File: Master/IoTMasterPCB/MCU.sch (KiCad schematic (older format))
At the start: 1 part

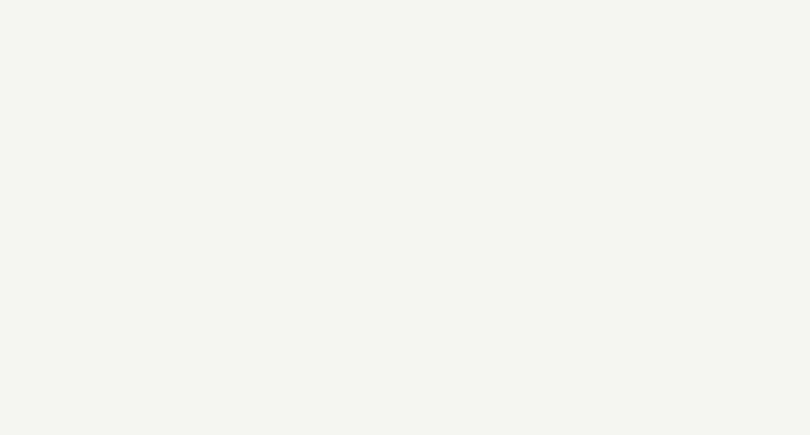
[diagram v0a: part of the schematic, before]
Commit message: Updated Master Board schematics. Added JTAG connector.
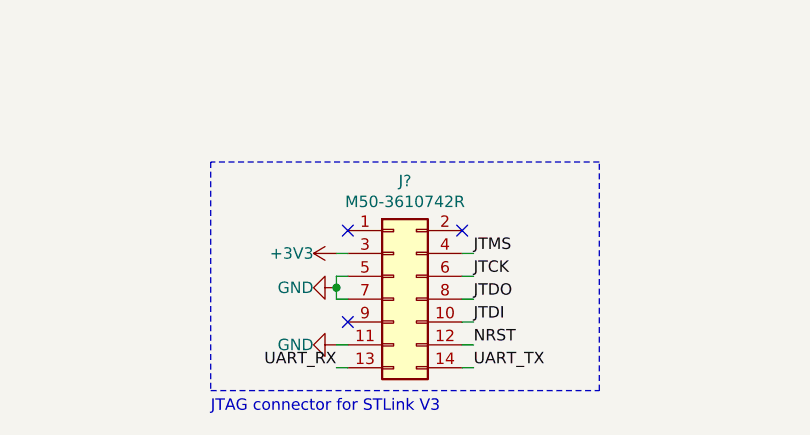
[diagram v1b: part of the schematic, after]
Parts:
- added J?: M50-3610742R, Personal_Misc:M50-3610742R, symbol Connector_Generic:Conn_02x07_Odd_Even
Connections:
- new net +3V3: J?.3 (Pin_3)
- new net GND: J?.11 (Pin_11), J?.5 (Pin_5), J?.7 (Pin_7)
- new net JTCK: J?.6 (Pin_6)
- new net JTDI: J?.10 (Pin_10)
- new net JTDO: J?.8 (Pin_8)
- new net JTMS: J?.4 (Pin_4)
- new net NRST: J?.12 (Pin_12)
- new net UART_RX: J?.13 (Pin_13)
- new net UART_TX: J?.14 (Pin_14)
- no-connect marks 0 -> 3
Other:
- note added: "JTAG connector for STLink V3"
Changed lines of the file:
@@
 $Descr A4 11693 8268
 encoding utf-8
-Sheet 2 7
+Sheet 2 6
 Title "IoT Master Board"
-Date "2020-11-01"
+Date "2020-11-28"
 Rev "1.0"
 Comp "University of Southern Denmark"
@@
 	0    1    1    0
 $EndComp
+$Comp
+L Connector_Generic:Conn_02x07_Odd_Even J?
+U 1 1 5FC223EF
+P 5950 7200
+F 0 "J?" H 6000 7717 50  0000 C CNN
+F 1 "M50-3610742R" H 6000 7626 50  0000 C CNN
+F 2 "Personal_Misc:M50-3610742R" H 5950 7200 50  0001 C CNN
+F 3 "~" H 5950 7200 50  0001 C CNN
+	1    5950 7200
+	1    0    0    -1
+$EndComp
+NoConn ~ 5750 6900
+NoConn ~ 6250 6900
+NoConn ~ 5750 7300
+$Comp
+L power:GND #PWR?
+U 1 1 5FC23999
+P 5700 7150
+F 0 "#PWR?" H 5700 6900 50  0001 C CNN
+F 1 "GND" V 5700 7050 50  0000 R CNN
+F 2 "" H 5700 7150 50  0001 C CNN
+F 3 "" H 5700 7150 50  0001 C CNN
+	1    5700 7150
+	0    1    1    0
+$EndComp
+Wire Wire Line
+	5750 7100 5700 7100
+Wire Wire Line
+	5700 7100 5700 7150
+Wire Wire Line
+	5700 7200 5750 7200
+Connection ~ 5700 7150
+Wire Wire Line
+	5700 7150 5700 7200
+$Comp
+L power:GND #PWR?
+U 1 1 5FC24573
+P 5700 7400
+F 0 "#PWR?" H 5700 7150 50  0001 C CNN
+F 1 "GND" V 5700 7300 50  0000 R CNN
+F 2 "" H 5700 7400 50  0001 C CNN
+F 3 "" H 5700 7400 50  0001 C CNN
+	1    5700 7400
+	0    1    1    0
+$EndComp
+Wire Wire Line
+	5700 7400 5750 7400
+$Comp
+L power:+3V3 #PWR?
+U 1 1 5FC24F27
+P 5700 7000
+F 0 "#PWR?" H 5700 6850 50  0001 C CNN
+F 1 "+3V3" V 5700 7100 50  0000 L CNN
+F 2 "" H 5700 7000 50  0001 C CNN
+F 3 "" H 5700 7000 50  0001 C CNN
+	1    5700 7000
+	0    -1   -1   0
+$EndComp
+Wire Wire Line
+	5700 7000 5750 7000
+Wire Wire Line
+	5750 7500 5700 7500
+Wire Wire Line
+	6300 7500 6250 7500
+Wire Wire Line
+	6300 7400 6250 7400
+Wire Wire Line
+	6300 7300 6250 7300
+Wire Wire Line
+	6300 7200 6250 7200
+Wire Wire Line
+	6300 7100 6250 7100
+Wire Wire Line
+	6300 7000 6250 7000
+Text Label 5700 7500 2    50   ~ 0
+UART_RX
+Text Label 6300 7500 0    50   ~ 0
+UART_TX
+Text Label 6300 7400 0    50   ~ 0
+NRST
+Text Label 6300 7300 0    50   ~ 0
+JTDI
+Text Label 6300 7200 0    50   ~ 0
+JTDO
+Text Label 6300 7100 0    50   ~ 0
+JTCK
+Text Label 6300 7000 0    50   ~ 0
+JTMS
+Wire Notes Line
+	5150 7600 6850 7600
+Wire Notes Line
+	6850 7600 6850 6600
+Wire Notes Line
+	6850 6600 5150 6600
+Wire Notes Line
+	5150 6600 5150 7600
+Text Notes 5150 7700 0    50   ~ 0
+JTAG connector for STLink V3
 $EndSCHEMATC

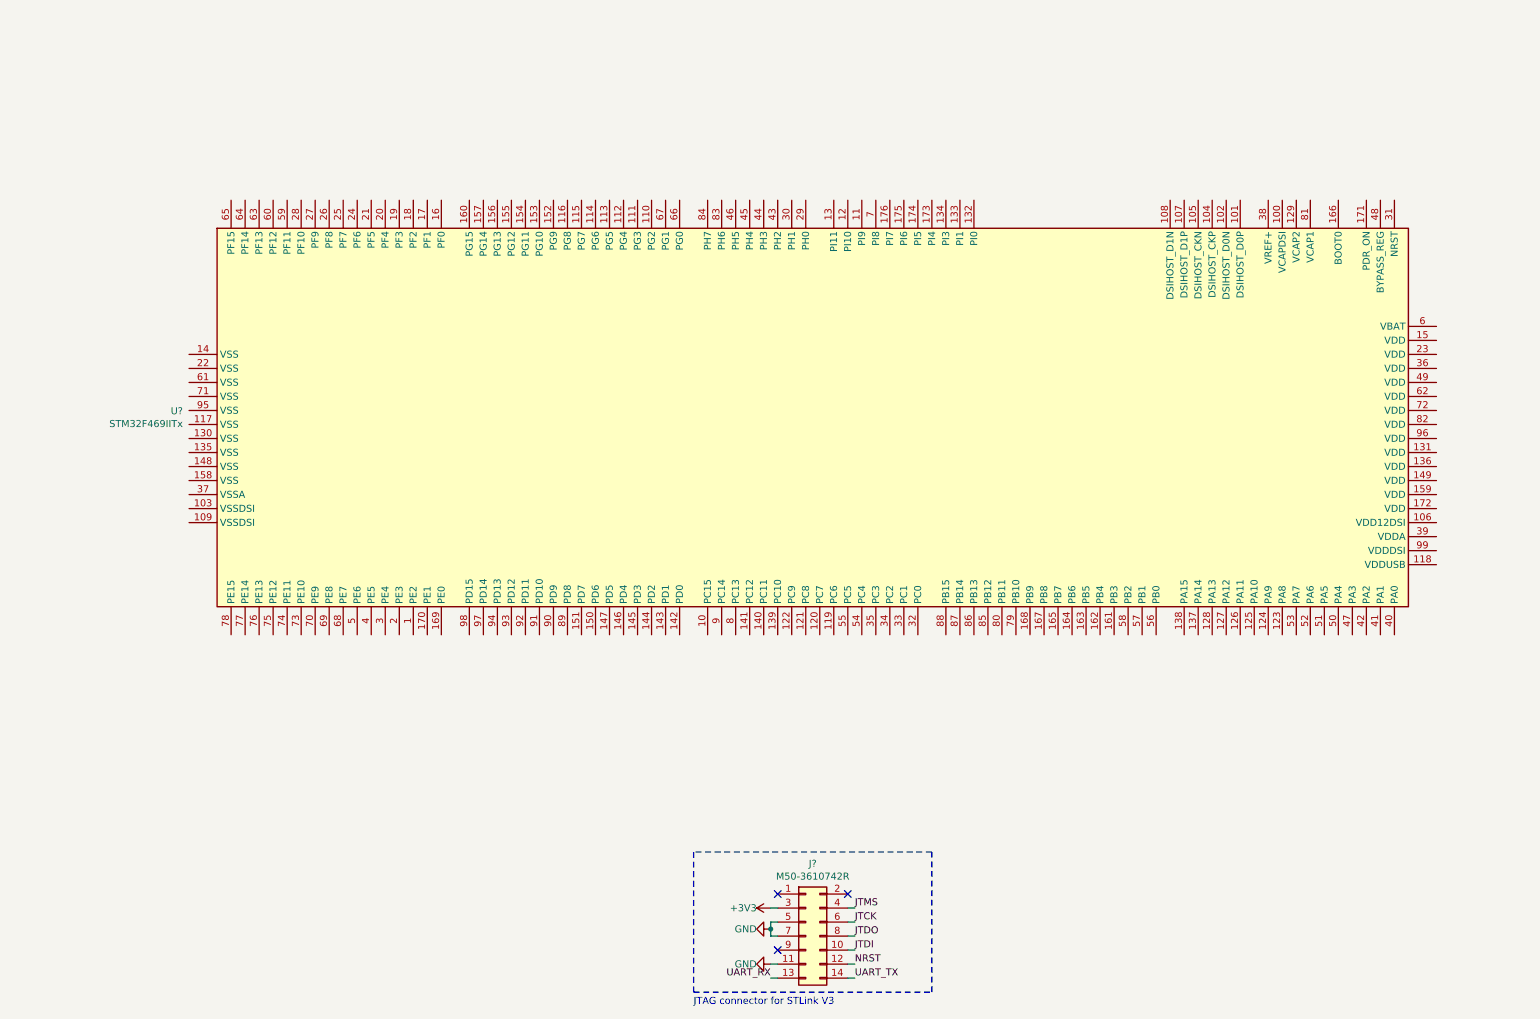
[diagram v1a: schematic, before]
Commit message: Work on Master Board schematics; added full Zigbee. Added RFID module. Added USB/power supply, as well as MCU decoupling.
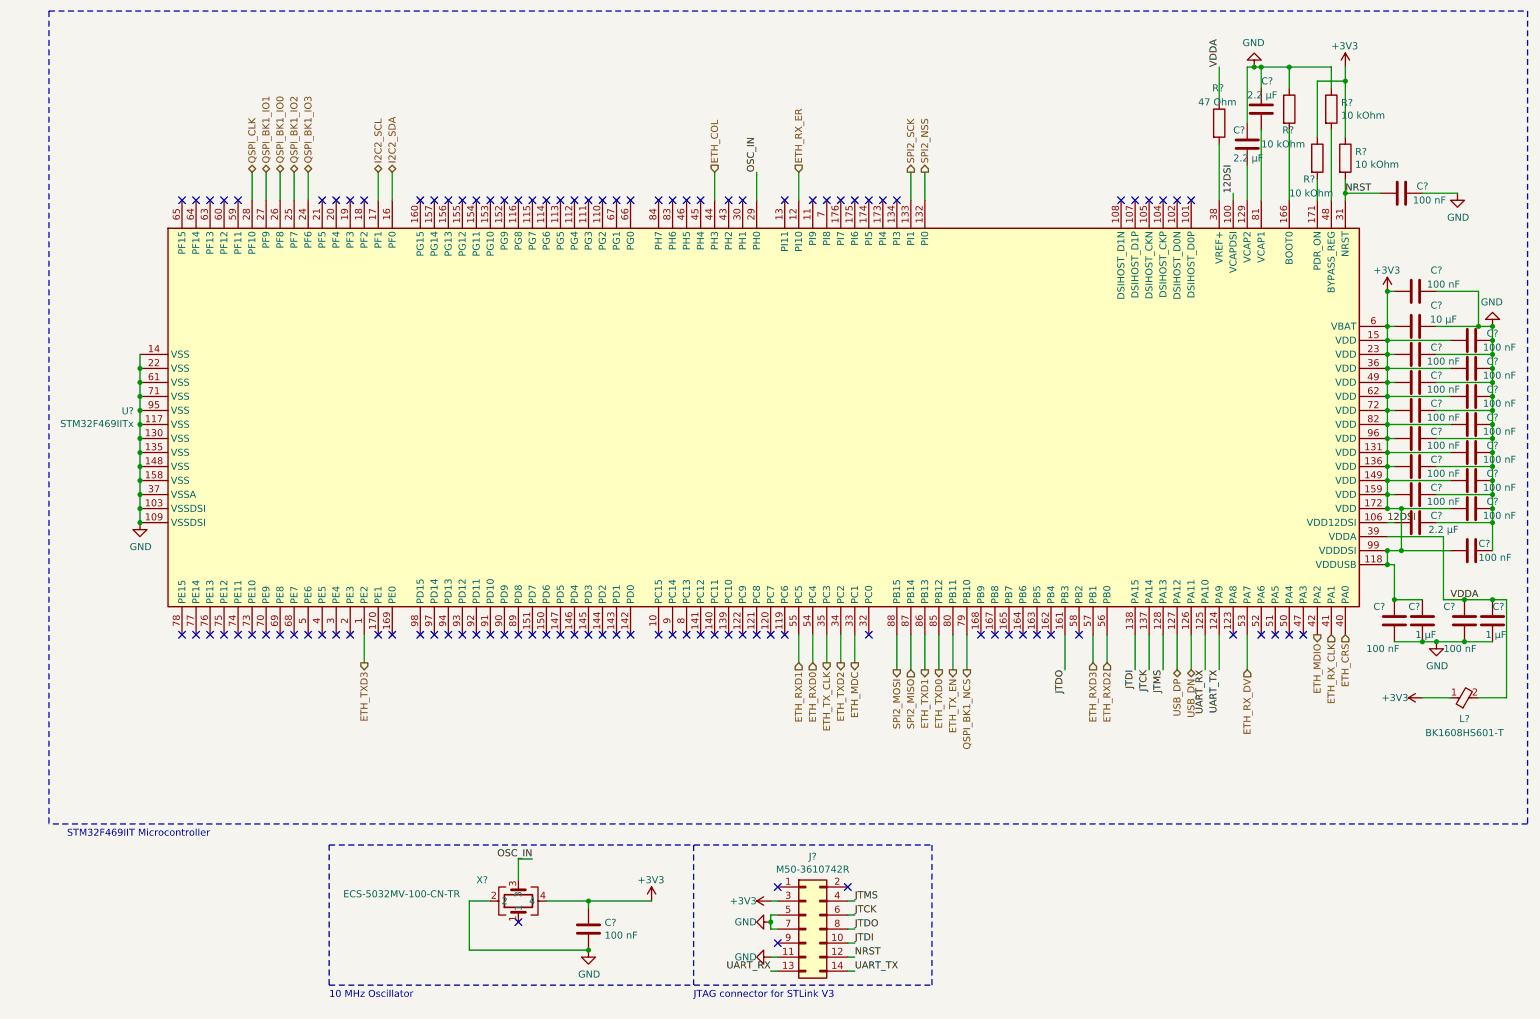
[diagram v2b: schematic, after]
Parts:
- removed U?: STM32F469IITx, Package_QFP:LQFP-176_24x24mm_P0.5mm, symbol MCU_ST_STM32F4:STM32F469IITx
- added C? (x3): 2.2 µF, Capacitor_SMD:C_0603_1608Metric, symbol Device:C
- added C? (x19): 100 nF, Capacitor_SMD:C_0603_1608Metric, symbol Device:C
- added C?: 10 µF, Capacitor_SMD:C_0603_1608Metric, symbol Device:C
- added C? (x2): 1 µF, Capacitor_SMD:C_0603_1608Metric, symbol Device:C
- added L?: BK1608HS601-T, Personal_Passives:BK1608HS601-T, symbol Personal_Passives:BK1608HS601-T
- added R?: 47 Ohm, Resistor_SMD:R_0603_1608Metric, symbol Device:R
- added R? (x4): 10 kOhm, Resistor_SMD:R_0603_1608Metric, symbol Device:R
- added U?: STM32F469IITx, Package_QFP:LQFP-176_24x24mm_P0.5mm, symbol MCU_ST_STM32F4:STM32F469IITx
- added X?: ECS-5032MV-100-CN-TR, Personal_Actives:ECS5032MV250CNTR, symbol Personal_Actives:ECS-5032MV-100-CN-TR
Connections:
- net +3V3: now also C?.1, C?.1, C?.1, C?.1, C?.2, C?.2, C?.2, C?.2, C?.2, C?.2, C?.2, C?.2, C?.2, C?.2, C?.2, C?.2, C?.2, C?.2, C?.2, L?.1, R?.1, R?.1, U?.118 (VDDUSB), U?.131 (VDD), U?.136 (VDD), U?.149 (VDD), U?.15 (VDD), U?.159 (VDD), U?.172 (VDD), U?.23 (VDD), U?.36 (VDD), U?.49 (VDD), U?.6 (VBAT), U?.62 (VDD), U?.72 (VDD), U?.82 (VDD), U?.96 (VDD), U?.99 (VDDDSI), X?.4
- net GND: now also C?.1, C?.1, C?.1, C?.1, C?.1, C?.1, C?.1, C?.1, C?.1, C?.1, C?.1, C?.1, C?.1, C?.1, C?.1, C?.1, C?.1, C?.1, C?.1, C?.2, C?.2, C?.2, C?.2, C?.2, C?.2, R?.1, R?.1, U?.103 (VSSDSI), U?.109 (VSSDSI), U?.117 (VSS), U?.130 (VSS), U?.135 (VSS), U?.14 (VSS), U?.148 (VSS), U?.158 (VSS), U?.22 (VSS), U?.37 (VSSA), U?.61 (VSS), U?.71 (VSS), U?.95 (VSS), X?.2
- net JTCK: now also U?.137 (PA14)
- net JTDI: now also U?.138 (PA15)
- net JTDO: now also U?.161 (PB3)
- net JTMS: now also U?.128 (PA13)
- net NRST: now also C?.2, R?.2, U?.31 (NRST)
- net UART_RX: now also U?.125 (PA10)
- net UART_TX: now also U?.124 (PA9)
- new net: C?.2, U?.129 (VCAP2)
- new net: C?.2, U?.81 (VCAP1)
- new net: R?.2, U?.38 (VREF+)
- new net: R?.2, U?.48 (BYPASS_REG)
- new net: R?.2, U?.166 (BOOT0)
- new net: R?.2, U?.171 (PDR_ON)
- new net 12DSI: C?.2, U?.100 (VCAPDSI), U?.106 (VDD12DSI)
- new net ETH_COL: U?.44 (PH3)
- new net ETH_CRS: U?.40 (PA0)
- new net ETH_MDC: U?.33 (PC1)
- new net ETH_MDIO: U?.42 (PA2)
- new net ETH_RXD0: U?.54 (PC4)
- new net ETH_RXD1: U?.55 (PC5)
- new net ETH_RXD2: U?.56 (PB0)
- new net ETH_RXD3: U?.57 (PB1)
- new net ETH_RX_CLK: U?.41 (PA1)
- new net ETH_RX_DV: U?.53 (PA7)
- new net ETH_RX_ER: U?.12 (PI10)
- new net ETH_TXD0: U?.85 (PB12)
- new net ETH_TXD1: U?.86 (PB13)
- new net ETH_TXD2: U?.34 (PC2)
- new net ETH_TXD3: U?.1 (PE2)
- new net ETH_TX_CLK: U?.35 (PC3)
- new net ETH_TX_EN: U?.80 (PB11)
- new net I2C2_SCL: U?.17 (PF1)
- new net I2C2_SDA: U?.16 (PF0)
- new net OSC_IN: U?.29 (PH0), X?.3
- new net QSPI_BK1_IO0: U?.26 (PF8)
- new net QSPI_BK1_IO1: U?.27 (PF9)
- new net QSPI_BK1_IO2: U?.25 (PF7)
- new net QSPI_BK1_IO3: U?.24 (PF6)
- new net QSPI_BK1_NCS: U?.79 (PB10)
- new net QSPI_CLK: U?.28 (PF10)
- new net SPI2_MISO: U?.87 (PB14)
- new net SPI2_MOSI: U?.88 (PB15)
- new net SPI2_NSS: U?.132 (PI0)
- new net SPI2_SCK: U?.133 (PI1)
- new net USB_DN: U?.126 (PA11)
- new net USB_DP: U?.127 (PA12)
- new net VDDA: C?.1, C?.1, L?.2, R?.1, U?.39 (VDDA)
- no-connect marks 3 -> 103
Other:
- note added: "10 MHz Oscillator"
- note added: "STM32F469IIT Microcontroller"
- moved on the sheet: J?

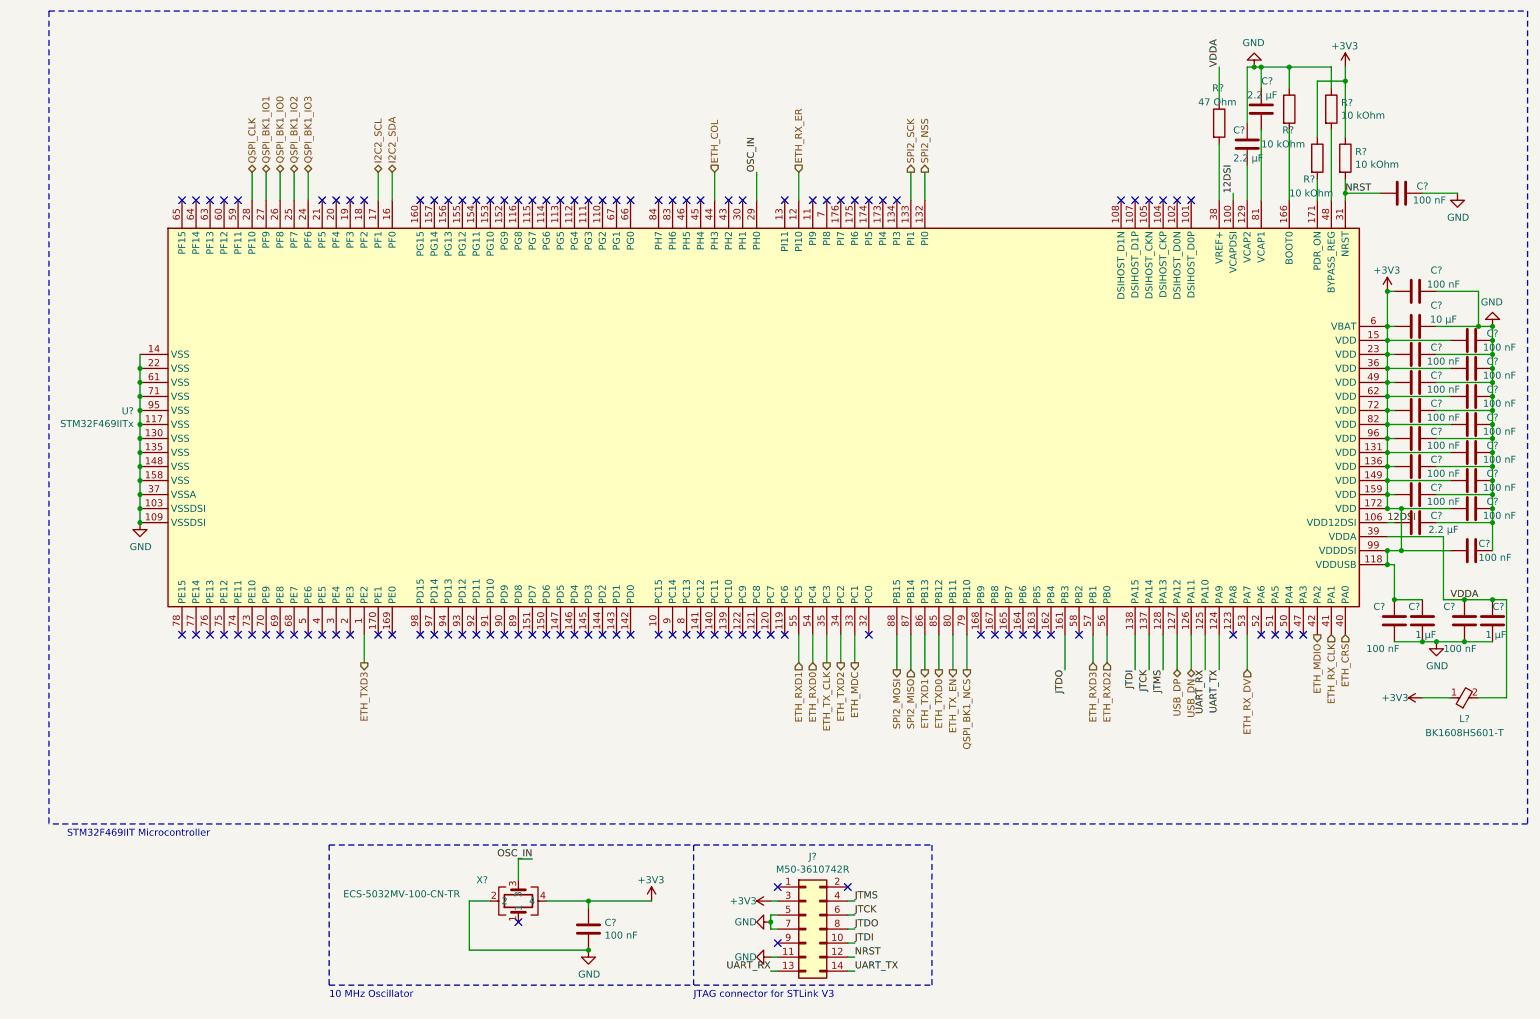
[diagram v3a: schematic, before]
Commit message: Finished RFID module sans antenna footprint. Added KSZ8081MNX and hierarchial connections.
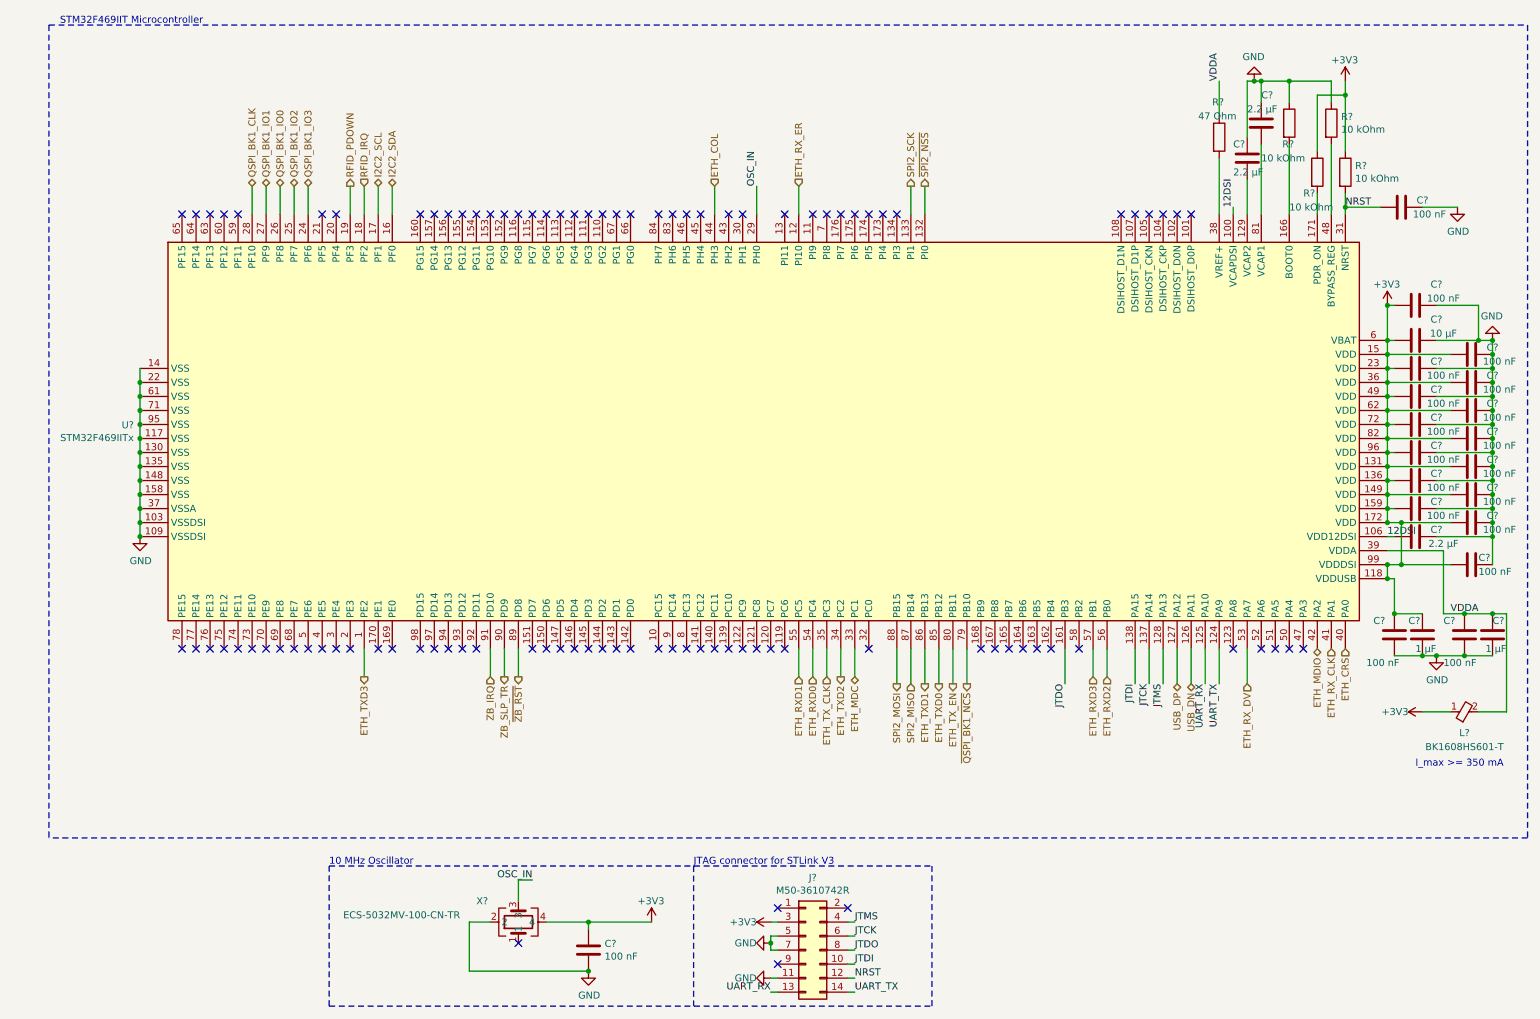
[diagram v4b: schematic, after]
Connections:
- net RFID_IRQ: now reaches U?.18 (PF2)
- net RFID_PDOWN: now reaches U?.19 (PF3)
- net ~ZB_RST: now reaches U?.89 (PD8)
- net ZB_SLP_TR: now reaches U?.90 (PD9)
- net ZB_IRQ: now reaches U?.91 (PD10)
- net QSPI_BK1_NCS renamed ~QSPI_BK1_NCS
- net QSPI_CLK renamed QSPI_BK1_CLK
- net SPI2_NSS renamed ~SPI2_NSS
- no-connect marks 103 -> 98
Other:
- note added: "I_max >= 350 mA"
- moved on the sheet: C?, J?, L?, R?, U?, X?
